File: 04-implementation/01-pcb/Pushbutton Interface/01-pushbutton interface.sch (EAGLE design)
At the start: 1 part

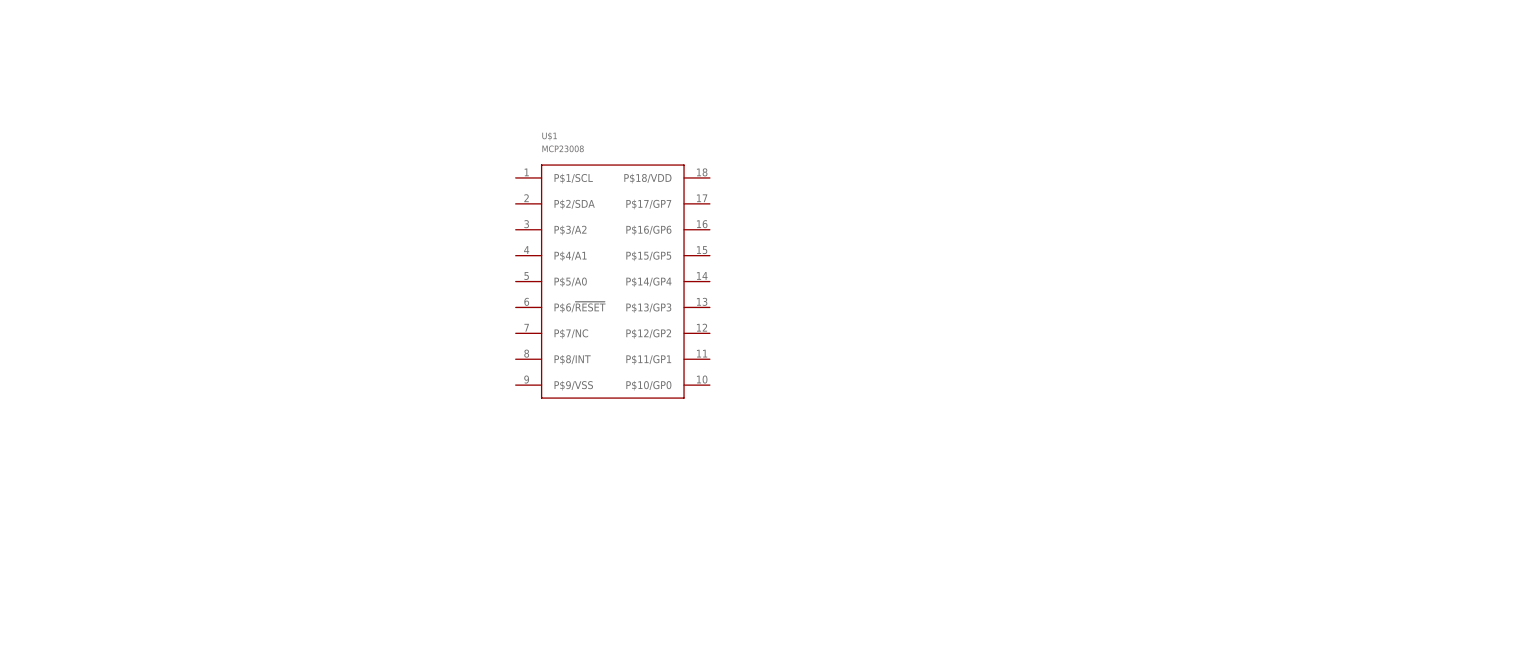
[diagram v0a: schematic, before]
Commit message: Add files for initial placement of pushbutton interface.
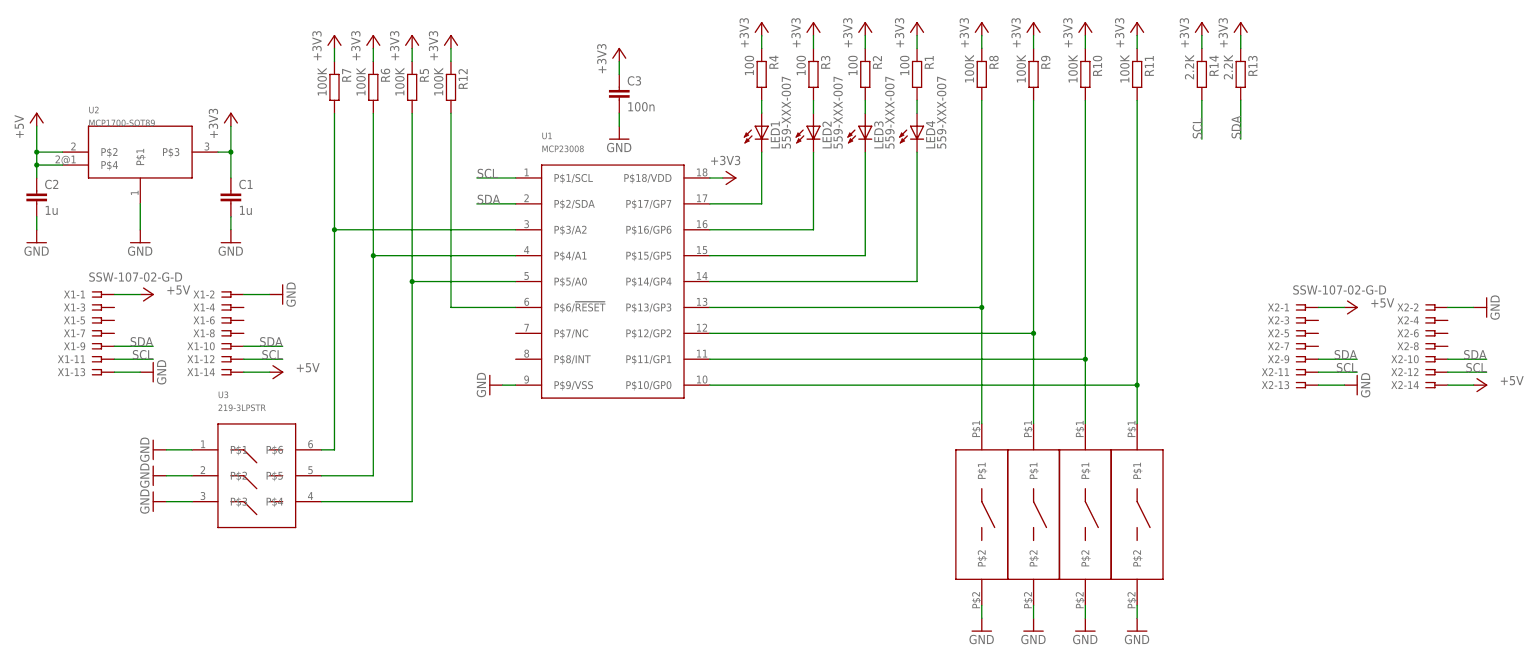
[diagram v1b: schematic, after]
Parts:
- removed U$1: MCP23008, MIDI Pushbutton Parts:MCP23008
- added C1, C2: 1u, rcl:C-EUC0805
- added C3: 100n, rcl:C-EUC0805
- added LED1, LED2, LED3, LED4: 559-XXX-007, MIDI router parts:559-XXX-007
- added R1, R2, R3, R4: 100, rcl:R-EU_R0805
- added R10, R11, R12, R5, R6, R7, R8, R9: 100K, rcl:R-EU_R0805
- added R13, R14: 2.2K, rcl:R-EU_R0805
- added SW1, SW2, SW3, SW4: PB-SWITCH, MIDI router parts:PB-SWITCH
- added U1: MCP23008, MIDI router parts:MCP23008
- added U2: MCP1700-SOT89, MIDI router parts:MCP1700-SOT89
- added U3: 219-3LPSTR, MIDI router parts:219-3LPSTR
- added X1, X2: SSW-107-02-G-D, MIDI router parts:SSW-107-02-G-D
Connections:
- new net +3V3: C1.1, C3.1, R1.1, R10.1, R11.1, R12.1, R13.1, R14.1, R2.1, R3.1, R4.1, R5.1, R6.1, R7.1, R8.1, R9.1, U1.P$18/VDD, U2.P$3
- new net +5V: C2.1, U2.P$2, U2.P$4, X1-1.1, X1-14.1, X2-1.1, X2-14.1
- new net GND: C1.2, C2.2, C3.2, SW1.P$2, SW2.P$2, SW3.P$2, SW4.P$2, U1.P$9/VSS, U2.P$1, U3.P$1, U3.P$2, U3.P$3, X1-13.1, X1-2.1, X2-13.1, X2-2.1
- new net N$1: R8.2, SW1.P$1, U1.P$13/GP3
- new net N$10: LED4.C, U1.P$14/GP4
- new net N$11: R7.2, U1.P$3/A2, U3.P$6
- new net N$12: R6.2, U1.P$4/A1, U3.P$5
- new net N$13: R5.2, U1.P$5/A0, U3.P$4
- new net N$14: R10.2, SW3.P$1, U1.P$11/GP1
- new net N$15: R11.2, SW4.P$1, U1.P$10/GP0
- new net N$16: R12.2, U1.P$6/!RESET
- new net N$2: R9.2, SW2.P$1, U1.P$12/GP2
- new net N$3: LED4.A, R1.2
- new net N$4: LED3.A, R2.2
- new net N$5: LED2.A, R3.2
- new net N$6: LED1.A, R4.2
- new net N$7: LED1.C, U1.P$17/GP7
- new net N$8: LED2.C, U1.P$16/GP6
- new net N$9: LED3.C, U1.P$15/GP5
- new net SCL: R14.2, U1.P$1/SCL, X1-11.1, X1-12.1, X2-11.1, X2-12.1
- new net SDA: R13.2, U1.P$2/SDA, X1-10.1, X1-9.1, X2-10.1, X2-9.1

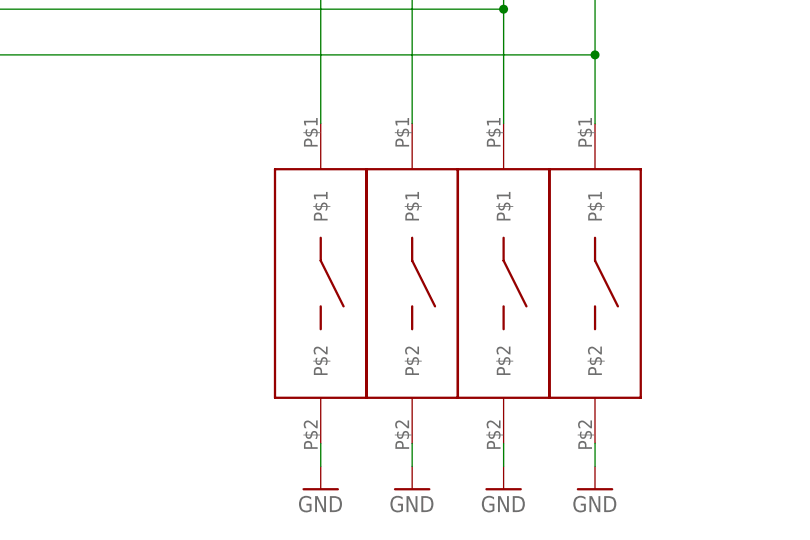
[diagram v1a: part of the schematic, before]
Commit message: Add files for pushbutton PCB.
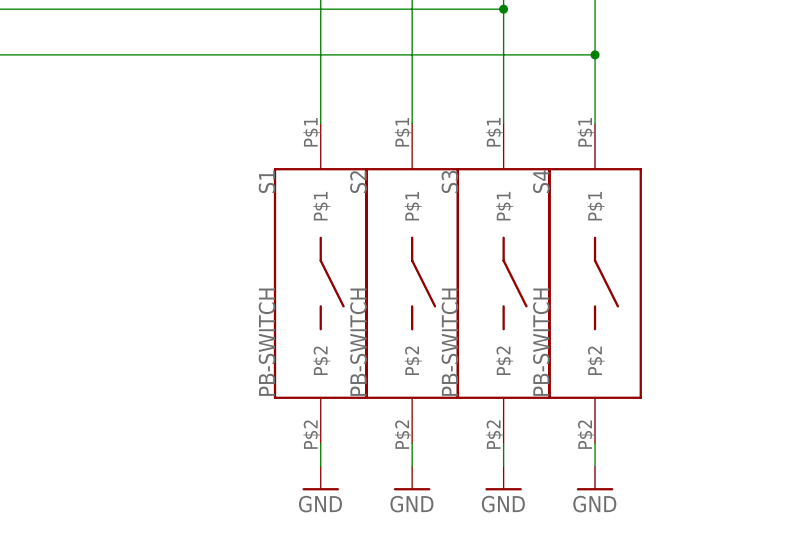
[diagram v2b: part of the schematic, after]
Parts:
- renumbered SW1 to S1, SW2 to S2, SW3 to S3, SW4 to S4
